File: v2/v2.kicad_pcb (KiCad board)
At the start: 2 copper layers, 95.2 x 95.2 mm, 67 parts, among them J1 cBUSoutV, J10 mcuTIEout, J11 USB_C_Receptacle_USB2.0, J12 Conn_01x06_Female, J2 cBUSinV, J3 cTIEoutV, J4 cTIEinV, J5 rBUSoutH, J6 cTIEoutH, J7 mcuTIEin, J8 cTIEinH, J9 rBUSinH, SW1 KeySwitch, SW10 KeySwitch, SW11 KeySwitch, SW12 KeySwitch, SW13 KeySwitch, SW14 KeySwitch, SW15 KeySwitch, SW16 KeySwitch, SW17 KeySwitch, SW18 KeySwitch, SW19 KeySwitch, SW2 KeySwitch, SW20 KeySwitch, SW21 KeySwitch, SW22 KeySwitch, SW23 KeySwitch, SW24 KeySwitch, SW25 KeySwitch, SW3 KeySwitch, SW4 KeySwitch, SW5 KeySwitch, SW6 KeySwitch, SW7 KeySwitch, SW8 KeySwitch, SW9 KeySwitch, U1 ItsyBitsy5V

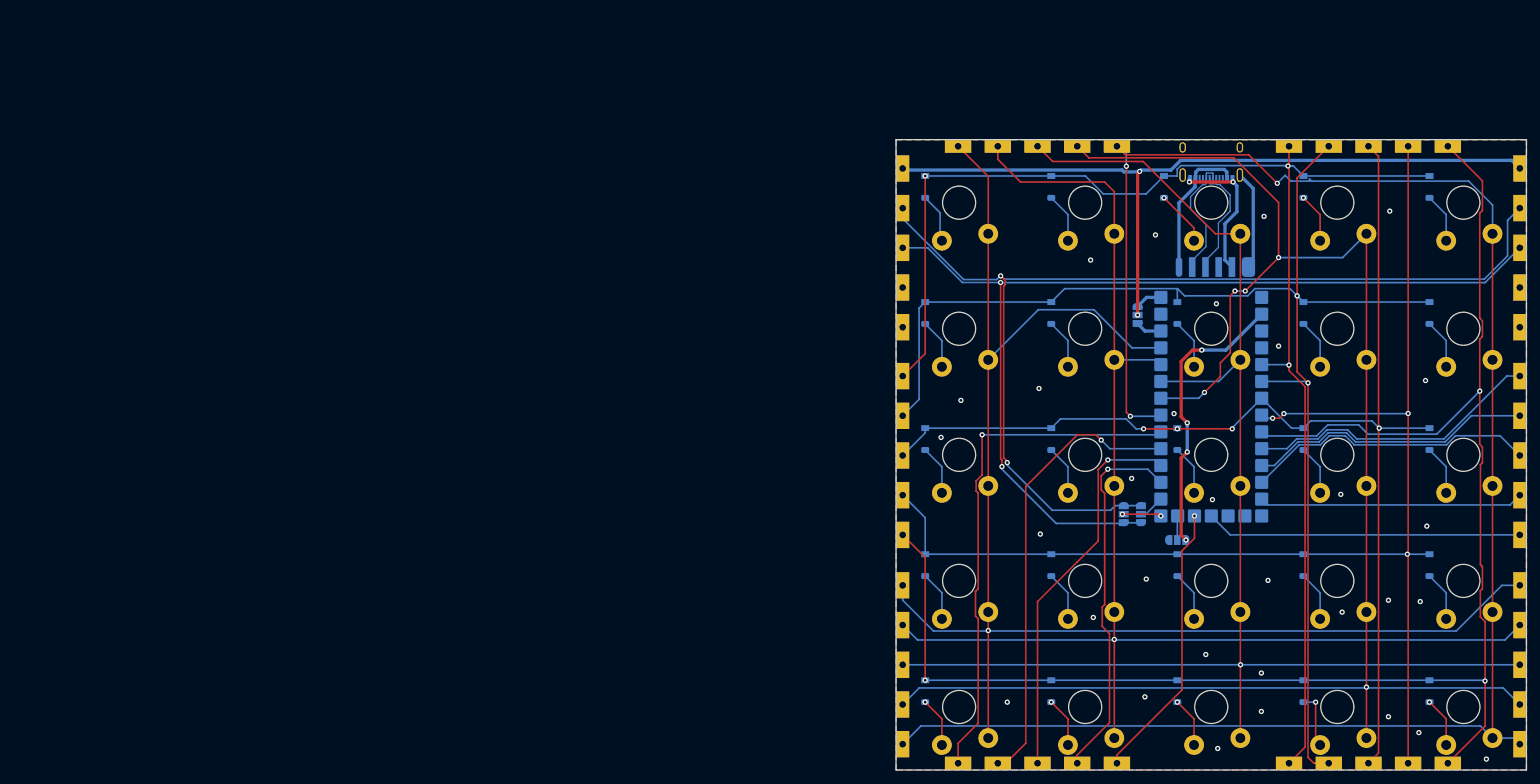
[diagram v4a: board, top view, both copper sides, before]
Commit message: Fix connection error in BUSs & TIEs
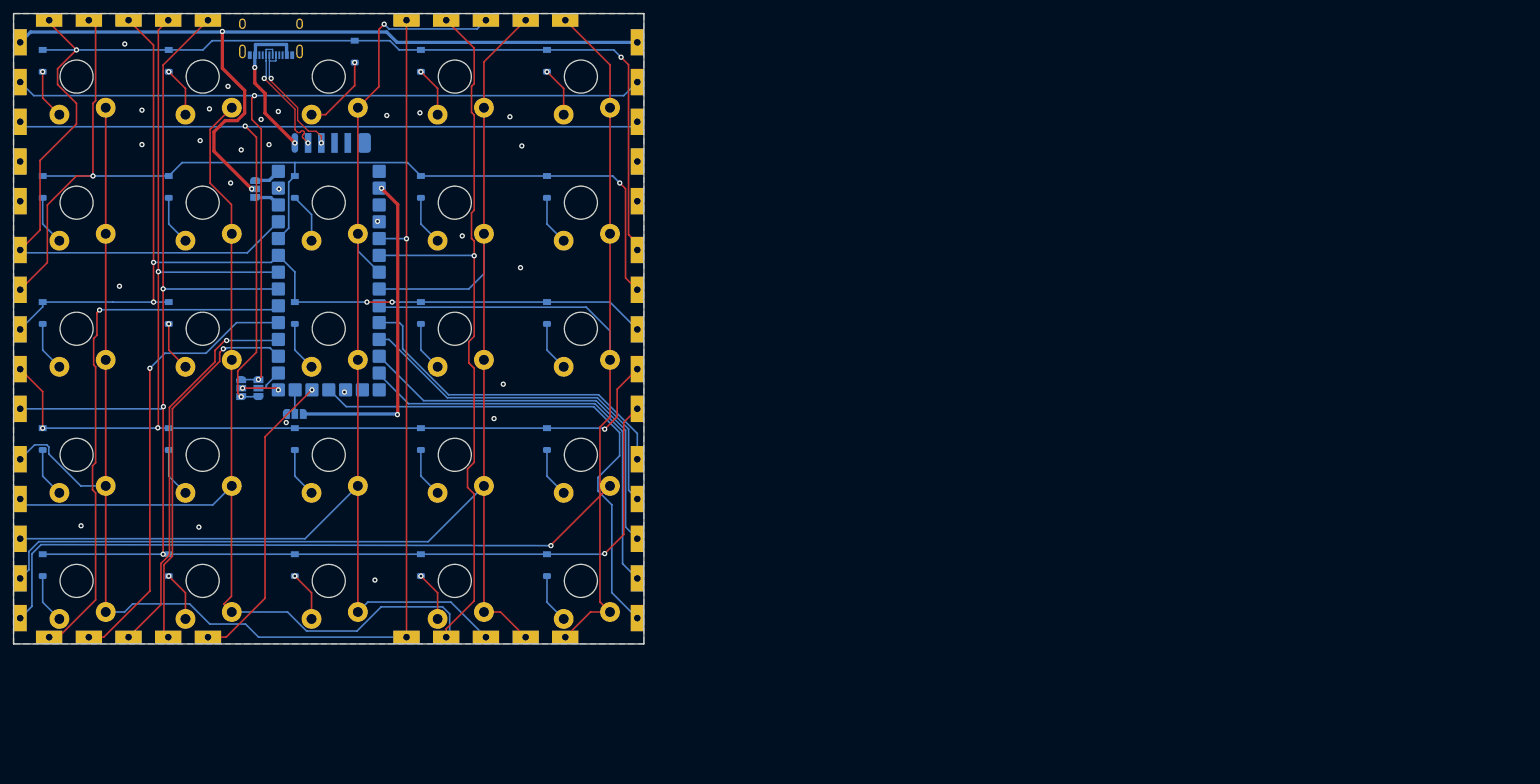
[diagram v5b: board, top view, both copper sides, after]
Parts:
- J1: value cBUSoutV -> rBUSoutV
- J2: value cBUSinV -> rBUSinV
- J5: value rBUSoutH -> cBUSoutH
- J6: value cTIEoutH -> rTIEoutH
- J8: value cTIEinH -> rTIEinH
- J9: value rBUSinH -> cBUSinH
- moved J11 143.3 mm to (58.3, 31.3)
- moved J6 142.7 mm to (19.4, 62.4)
- moved J8 142.7 mm to (112.7, 62.4)
- moved J1 138.7 mm to (22.8, 28.6)
- moved J2 138.7 mm to (22.8, 121.9)
- moved J12 134.9 mm to (73.4, 46.7)
- moved D10 134.7 mm to (100.0, 54.8)
- moved D12 134.7 mm to (42.9, 73.9)
- moved D15 134.7 mm to (100.0, 73.9)
- moved D17 134.7 mm to (42.9, 92.9)
- moved D2 134.7 mm to (42.9, 35.8)
- moved D20 134.7 mm to (100.0, 92.9)
- moved D22 134.7 mm to (42.9, 112.0)
- moved D25 134.7 mm to (100.0, 112.0)
- moved D5 134.7 mm to (100.0, 35.8)
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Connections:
- J1 pad 1: /b0c1 -> /b0r1
- J1 pad 2: /b0c2 -> /b0r2
- J1 pad 3: /b0c3 -> /b0r3
- J1 pad 4: /b0c4 -> /b0r4
- J1 pad 5: /b0c5 -> /b0r5
- J11 pad A1: /USB_GND -> GND
- J11 pad A12: /USB_GND -> GND
- J11 pad B1: /USB_GND -> GND
- J11 pad B12: /USB_GND -> GND
- J11 pad S1: /UBS_SHEILD -> GND
- J12 pad 5: /USB_GND -> GND
- J12 pad 6: /UBS_SHEILD -> GND
- J2 pad 1: /b1c1 -> /b1r1
- J2 pad 2: /b1c2 -> /b1r2
- J2 pad 3: /b1c3 -> /b1r3
- J2 pad 4: /b1c4 -> /b1r4
- J2 pad 5: /b1c5 -> /b1r5
- J3 pad 1: /b0r1 -> /b0c1
- J3 pad 2: /b0r2 -> /b0c2
- J3 pad 3: /b0r3 -> /b0c3
- J3 pad 4: /b0r4 -> /b0c4
- J3 pad 5: /b0r5 -> /b0c5
- J4 pad 1: /b0r1 -> /b0c1
- J4 pad 2: /b0r2 -> /b0c2
- J4 pad 3: /b0r3 -> /b0c3
- J4 pad 4: /b0r4 -> /b0c4
- J4 pad 5: /b0r5 -> /b0c5
- J5 pad 1: /b0r1 -> /b0c1
- J5 pad 2: /b0r2 -> /b0c2
- J5 pad 3: /b0r3 -> /b0c3
- J5 pad 4: /b0r4 -> /b0c4
- J5 pad 5: /b0r5 -> /b0c5
- J6 pad 1: /b0c1 -> /b0r1
- J6 pad 2: /b0c2 -> /b0r2
- J6 pad 3: /b0c3 -> /b0r3
- J6 pad 4: /b0c4 -> /b0r4
- J6 pad 5: /b0c5 -> /b0r5
- J8 pad 1: /b0c1 -> /b0r1
- J8 pad 2: /b0c2 -> /b0r2
- J8 pad 3: /b0c3 -> /b0r3
- J8 pad 4: /b0c4 -> /b0r4
- J8 pad 5: /b0c5 -> /b0r5
- J9 pad 1: /b1r1 -> /b1c1
- J9 pad 2: /b1r2 -> /b1c2
- J9 pad 3: /b1r3 -> /b1c3
- J9 pad 4: /b1r4 -> /b1c4
- J9 pad 5: /b1r5 -> /b1c5
- U1 pad 10: /b1r1 -> /b1c1
- U1 pad 11: /b1r2 -> /b1c2
- U1 pad 12: /b1r3 -> /b1c3
- U1 pad 13: /b1r4 -> /b1c4
- U1 pad 16: unconnected-(U1-Pad16) -> GND
- U1 pad 17: /b1r5 -> /b1c5
- U1 pad 18: /b1c5 -> /b1r5
- U1 pad 22: /b1c4 -> /b1r4
- U1 pad 23: /b1c3 -> /b1r3
- U1 pad 24: /b1c2 -> /b1r2
- U1 pad 25: /b1c1 -> /b1r1
- U1 pad 26: /b0c5 -> /b0r5
- U1 pad 27: /b0c4 -> /b0r4
- U1 pad 28: /b0c3 -> /b0r3
- U1 pad 29: /b0c2 -> /b0r2
- U1 pad 30: /b0c1 -> /b0r1
- U1 pad 5: /b0r1 -> /b0c1
- U1 pad 6: /b0r2 -> /b0c2
- U1 pad 7: /b0r3 -> /b0c3
- U1 pad 8: /b0r4 -> /b0c4
- U1 pad 9: /b0r5 -> /b0c5
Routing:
- net /b0c4: track 261.4 -> 200.2 mm, vias 5 -> 0
- net /b0c2: track 206.6 -> 265.7 mm
- net /b0c5: track 285.1 -> 245.0 mm, vias 3 -> 1
- net /b0r2: track 206.3 -> 166.4 mm
- net /b1c5: track 42.2 -> 78.4 mm, vias 1 -> 0
- net /b1r1: track 44.7 -> 79.1 mm, vias 0 -> 1
- net /b0r3: track 182.2 -> 149.6 mm
- net /b0c3: track 218.9 -> 190.3 mm
- net /b1c1: track 78.9 -> 51.9 mm, vias 1 -> 0
- net /b1r2: track 43.2 -> 68.0 mm, vias 0 -> 1
- net /USB_GND: track 21.8 -> 0.00 mm, vias 2 -> 0
- net /mTXsRX: track 159.2 -> 141.4 mm
- net /b1r4: track 40.0 -> 55.5 mm, vias 0 -> 1
- net /b0r4: track 202.4 -> 186.9 mm
- net /b0c1: track 223.2 -> 238.6 mm
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
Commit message: Tweaks & Cleanup
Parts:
- moved J12 0.95 mm to (73.4, 45.7)
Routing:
- net /mRXsTX: track 137.3 -> 135.7 mm
- net /mTXsRX: track 141.4 -> 139.9 mm
- net GND: vias 27 -> 37

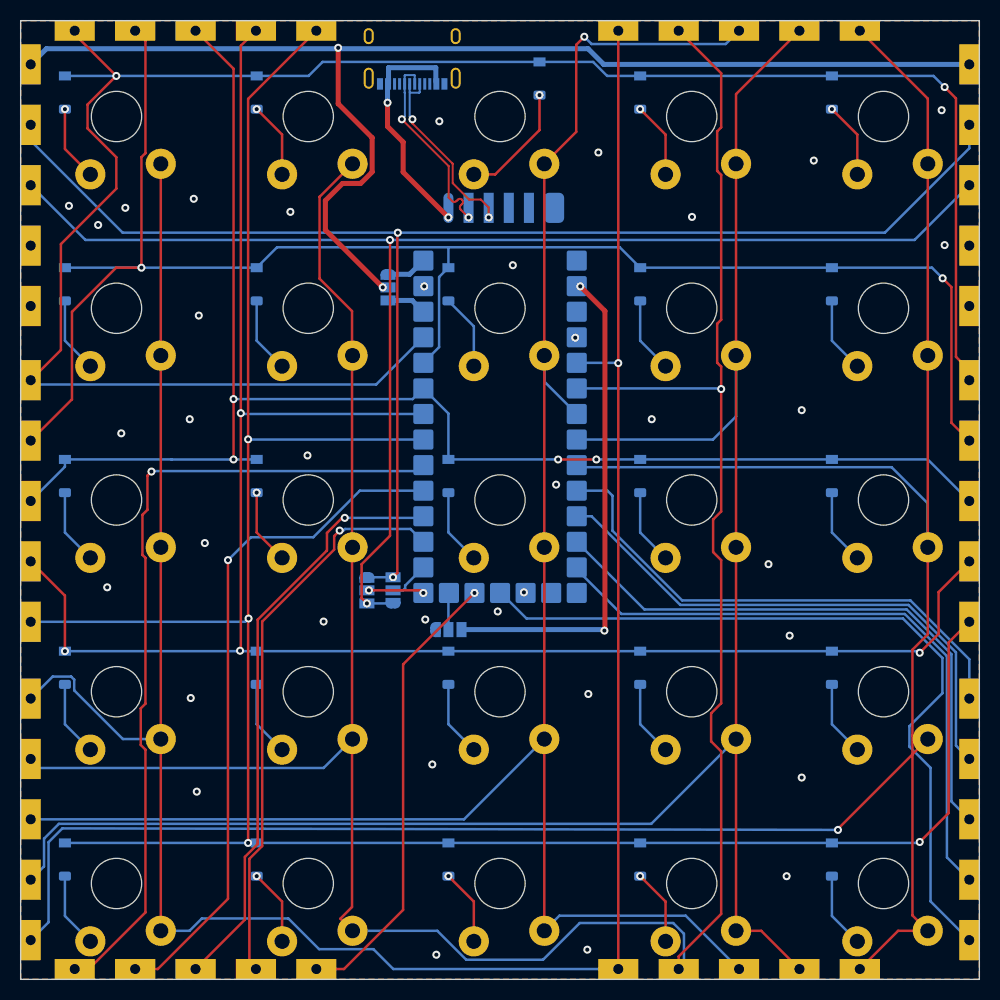
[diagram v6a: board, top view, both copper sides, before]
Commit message: Add mounting holes, tweak gound plane
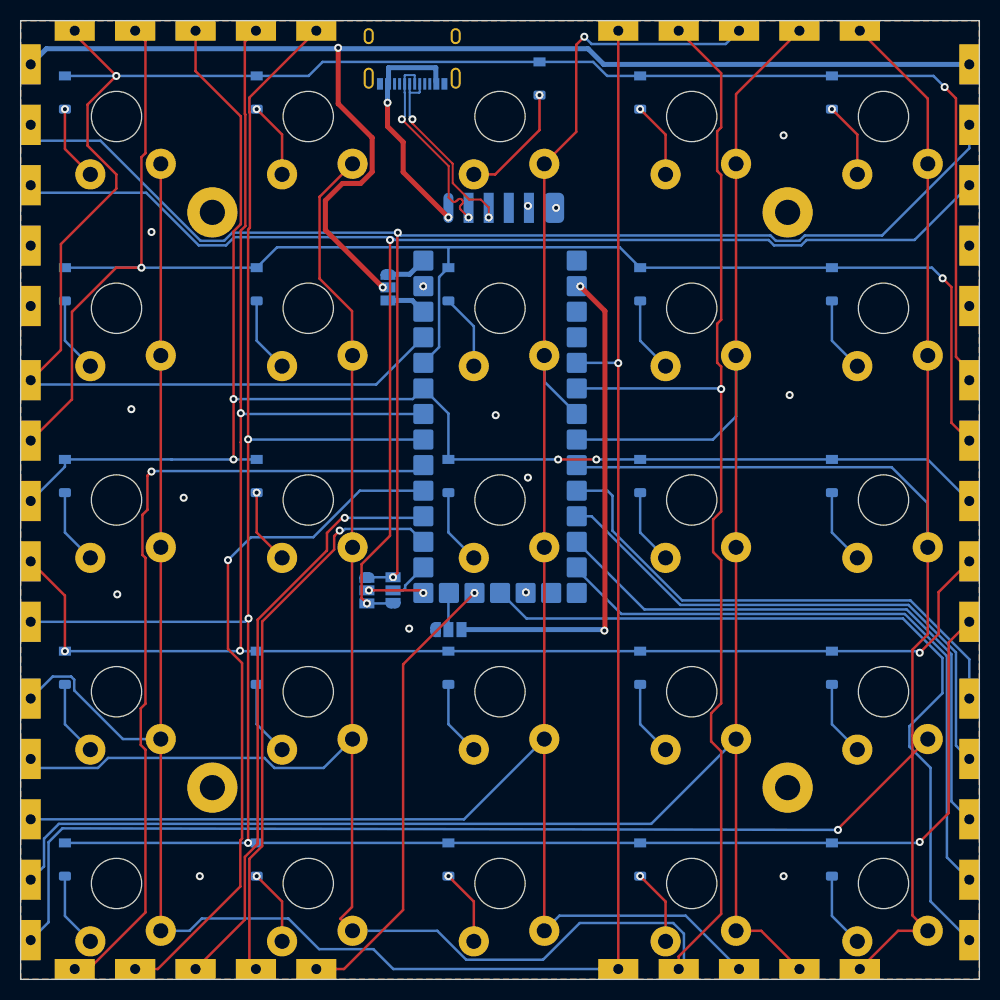
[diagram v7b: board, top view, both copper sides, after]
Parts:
- added H1: MountingHole, ProjectLibrary:MountingHole_Screw_2.5mm, F.Cu at (38.5, 104.8)
- added H2: MountingHole, ProjectLibrary:MountingHole_Screw_2.5mm, F.Cu at (95.6, 104.8)
- added H3: MountingHole, ProjectLibrary:MountingHole_Screw_2.5mm, F.Cu at (95.6, 47.7)
- added H4: MountingHole, ProjectLibrary:MountingHole_Screw_2.5mm, F.Cu at (38.5, 47.7)
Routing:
- net /mTXsRX: track 139.9 -> 141.2 mm
- net /b1r2: track 68.0 -> 69.2 mm
- net /mRXsTX: track 135.7 -> 136.8 mm
- net /b0c2: track 265.7 -> 266.5 mm
- net /b0r3: track 149.6 -> 150.2 mm
- net GND: vias 37 -> 15

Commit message: Optimise and reroute after first order feedback. Also add ordered files archive.
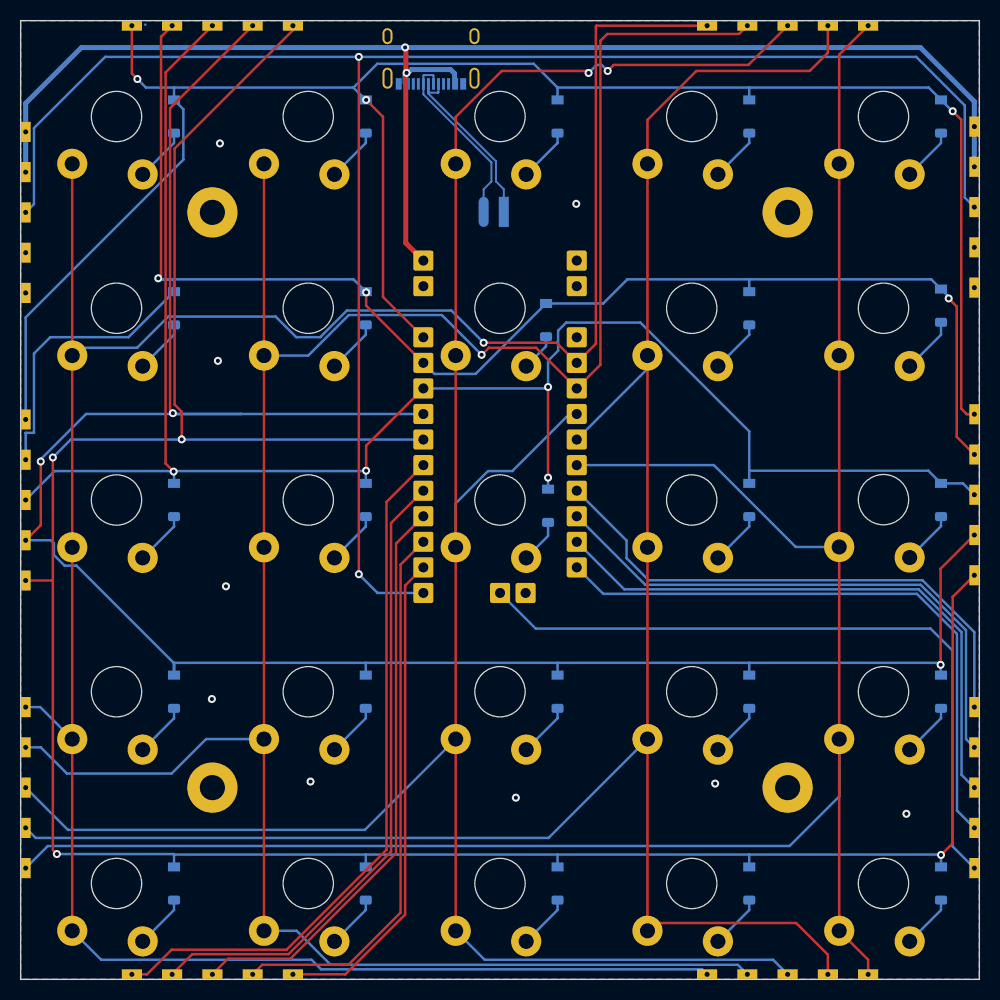
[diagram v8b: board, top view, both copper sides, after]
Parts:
- removed JP1, JP2, JP3, JP4: SolderJumper_3_Open, ProjectLibrary:SolderJumper-3_P1.3mm_Open_RoundedPad1.0x1.5mm_No_Silk
- J12: value Conn_01x06_Female -> Conn_01x02_Female
- moved D11 11.1 mm to (34.7, 76.3)
- moved D12 11.1 mm to (53.7, 76.3)
- moved D15 11.1 mm to (110.9, 76.3)
- moved D1 11.1 mm to (34.7, 38.2)
- moved D16 11.1 mm to (34.7, 95.3)
- moved D17 11.1 mm to (53.7, 95.3)
- moved D2 11.1 mm to (53.7, 38.2)
- moved D20 11.1 mm to (110.9, 95.3)
- moved D21 11.1 mm to (34.7, 114.4)
- moved D22 11.1 mm to (53.7, 114.4)
- moved D25 11.1 mm to (110.9, 114.4)
- moved D5 11.1 mm to (110.9, 38.2)
- moved D6 11.1 mm to (34.7, 57.2)
- moved D7 11.1 mm to (53.7, 57.2)
- moved D18 11.1 mm to (72.8, 95.3)
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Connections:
- J10 pad 2: /mTXsRX -> +VDC
- J10 pad 3: /mRXsTX -> /MCU_DATA
- J11 pad A4: /USB_VCC -> +VDC
- J11 pad A9: /USB_VCC -> +VDC
- J11 pad B4: /USB_VCC -> +VDC
- J11 pad B9: /USB_VCC -> +VDC
- J12 pad 1: /USB_VCC -> /USB_D-
- J12 pad 2: /USB_D- -> /USB_D+
- J7 pad 2: /mTXsRX -> +VDC
- J7 pad 3: /mRXsTX -> /MCU_DATA
- U1 pad 20: Net-(JP4-Pad2) -> /MCU_DATA
- U1 pad 21: Net-(JP3-Pad2) -> /b1r5
- U1 pad 33: Net-(JP2-Pad3) -> +VDC
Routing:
- net /MCU_DATA: track 0.00 -> 175.2 mm, vias 0 -> 2
- net /mTXsRX: track 141.2 -> 0.00 mm, vias 2 -> 0
- net /mRXsTX: track 136.8 -> 0.00 mm, vias 2 -> 0
- net +5V: track 49.5 -> 0.00 mm, vias 2 -> 0
- net /b0c3: track 190.3 -> 220.6 mm, vias 1 -> 2
- net /b0c5: track 245.0 -> 215.6 mm, vias 1 -> 0
- net /b0r4: track 186.9 -> 215.5 mm, vias 4 -> 3
- net /b0c2: track 266.5 -> 239.3 mm
- net /b0r3: track 150.2 -> 175.7 mm
- net /USB_VCC: track 23.5 -> 0.00 mm, vias 2 -> 0
- net /b0r5: track 231.6 -> 249.2 mm
- net +VDC: track 125.1 -> 142.2 mm
- net /b0r1: track 200.7 -> 191.2 mm, vias 2 -> 3
- net /b1r1: track 79.1 -> 70.2 mm, vias 1 -> 0
- net /b1c5: track 78.4 -> 69.8 mm
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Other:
- board text added: "JLCJLCJLCJLC"
- board text added: "THIS SIDE DOWN"
